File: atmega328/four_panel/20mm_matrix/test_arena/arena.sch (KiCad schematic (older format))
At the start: 35 parts, among them P1 CONN15, P10 CONN_2X2, P11 CONN_2X2, P12 CONN_2X2, P13 CONN_2X2, P14 CONN_2X2, P15 CONN_2X2, P16 CONN_2X2, P17 CONN_2X2, P18 CONN_2X2, P19 CONN_2X2, P2 CONN15, P20 CONN_2X2, P21 CONN_2X2, P22 CONN_20X2, P23 CONN_30X2, P24 CONN_2, P3 CONN15, P4 CONN15, P5 CONN15, P6 CONN15, P7 CONN_2X2, P8 CONN_2X2, P9 CONN_2X2

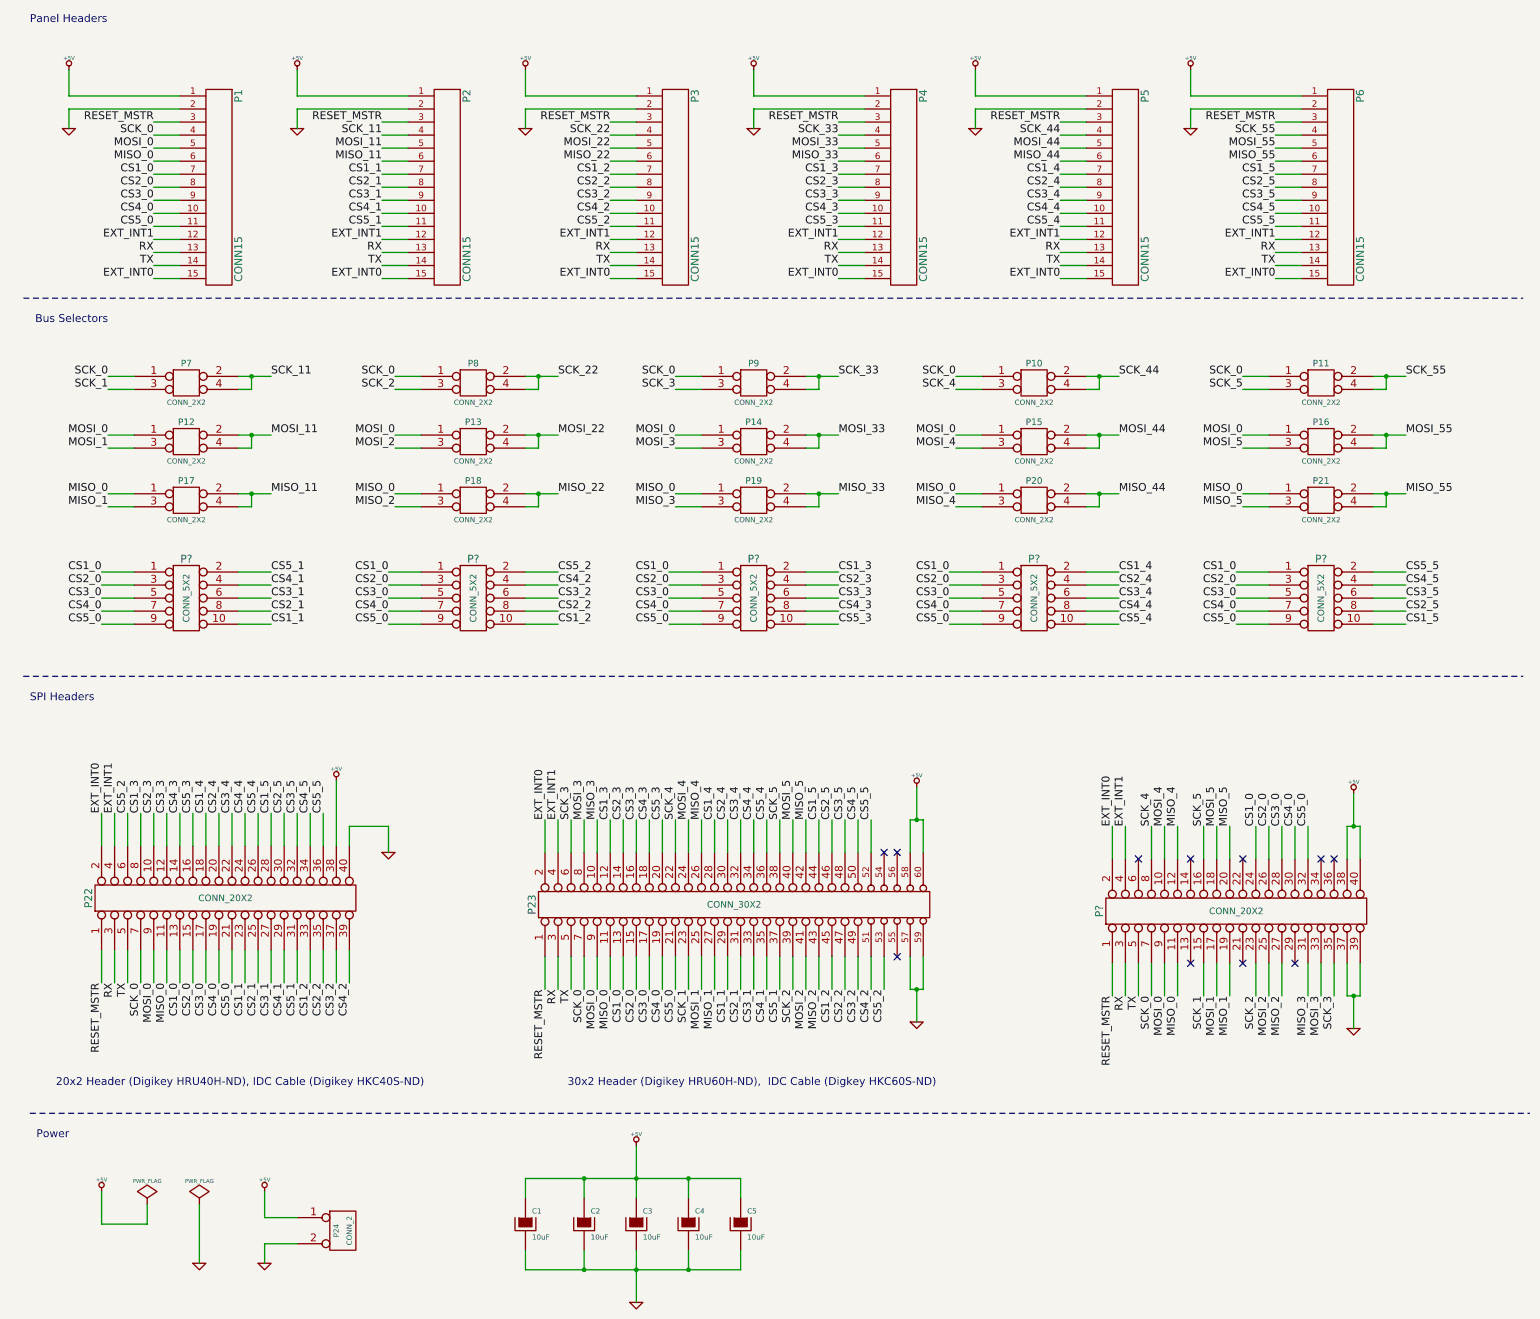
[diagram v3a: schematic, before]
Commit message: Added common CS SPI header to 4x20mm max6960 test arena. Fixed minor issue with 4x20mm atmega328 test arena.
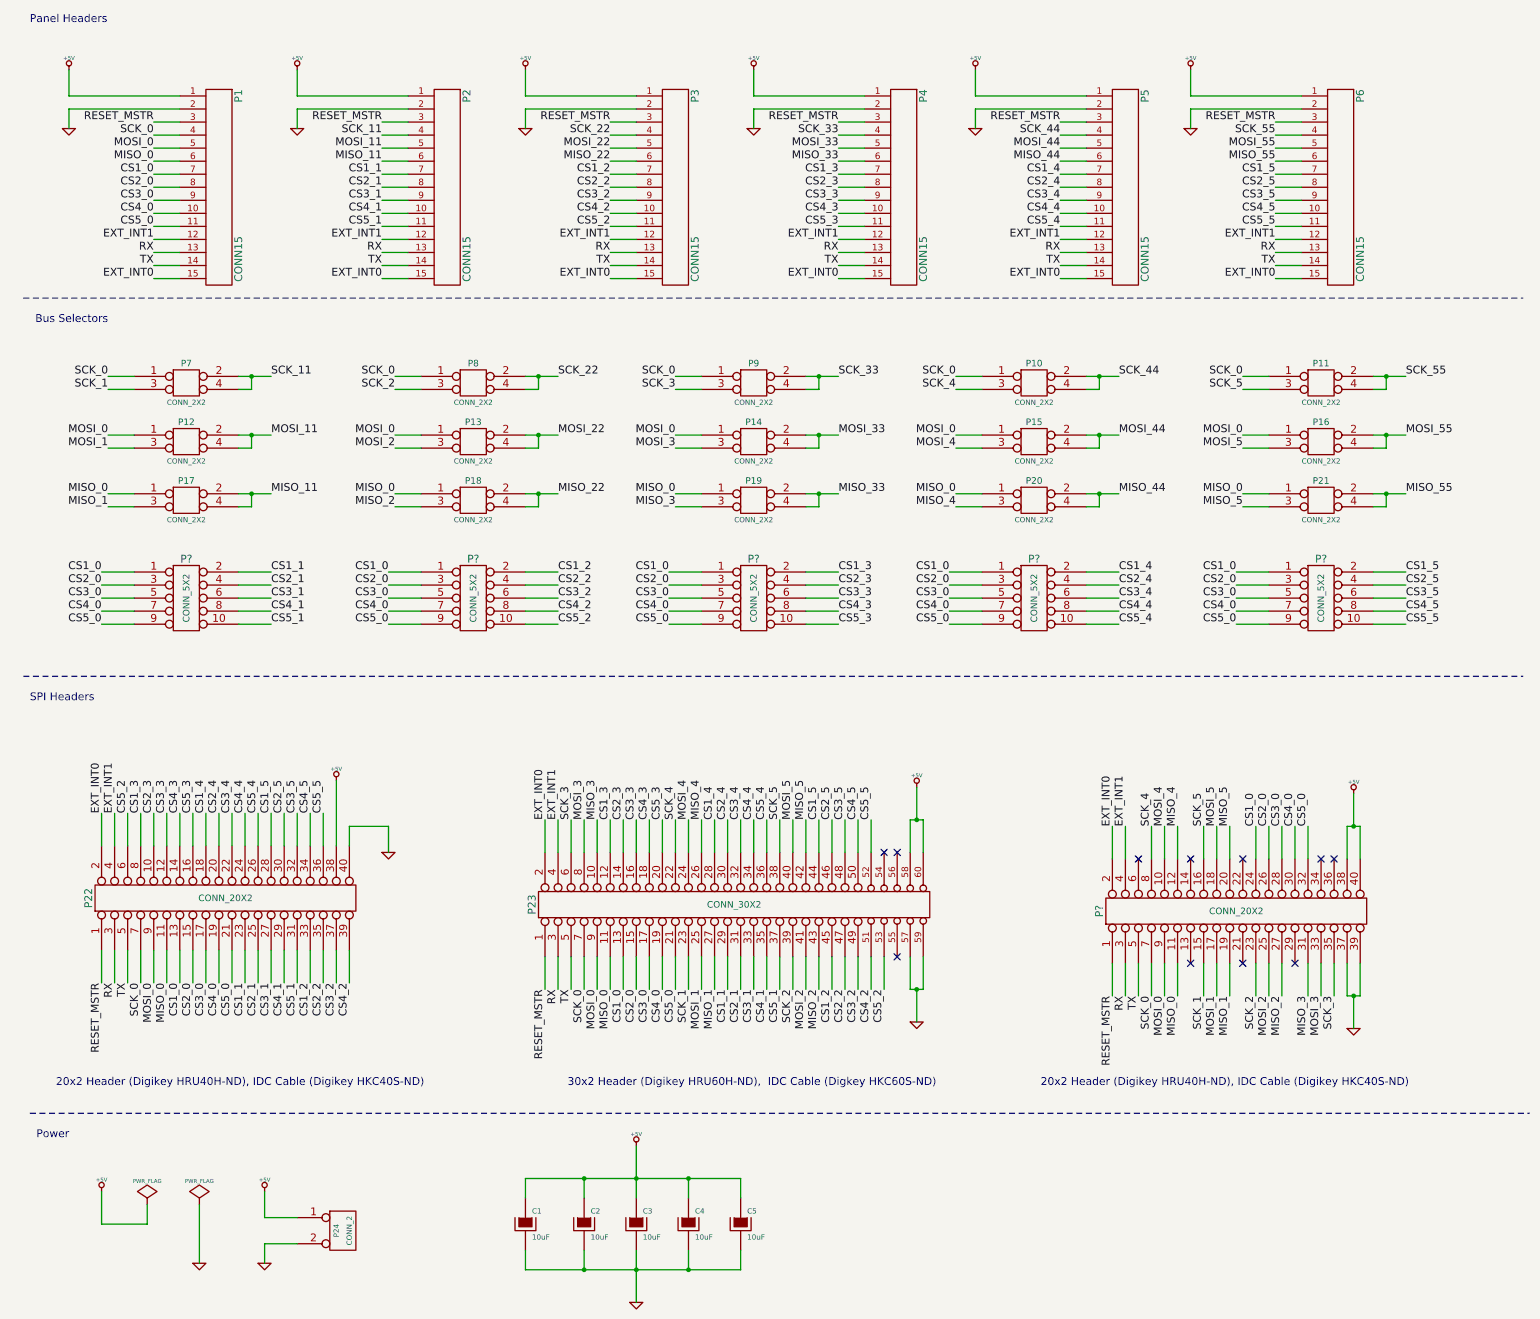
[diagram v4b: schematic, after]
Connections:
- net CS1_1: now also P?.2; no longer P?.10
- net CS1_2: now also P?.2; no longer P?.10
- net CS1_5: now also P?.2; no longer P?.10
- net CS2_1: now also P?.4; no longer P?.8
- net CS2_2: now also P?.4; no longer P?.8
- net CS2_5: now also P?.4; no longer P?.8
- net CS4_1: now also P?.8; no longer P?.4
- net CS4_2: now also P?.8; no longer P?.4
- net CS4_5: now also P?.8; no longer P?.4
- net CS5_1: now also P?.10; no longer P?.2
- net CS5_2: now also P?.10; no longer P?.2
- net CS5_5: now also P?.10; no longer P?.2
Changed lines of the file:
@@
 NoConn ~ 7200 7800
 Wire Wire Line
-	7300 6750 7400 6750
+	7300 6750 7350 6750
+Wire Wire Line
+	7350 6750 7400 6750
 Wire Wire Line
 	7350 6750 7350 6500
 Connection ~ 7350 6750
 Wire Wire Line
-	7300 8050 7400 8050
+	7300 8050 7350 8050
+Wire Wire Line
+	7350 8050 7400 8050
 Wire Wire Line
 	7350 8050 7350 8300
@@
 	1350 3450 1150 3450
 Wire Wire Line
-	2150 3350 2400 3350
+	2150 3350 2250 3350
+Wire Wire Line
+	2250 3350 2400 3350
 Wire Wire Line
 	2250 3350 2250 3450
@@
 	2250 3900 2250 3800
 Wire Wire Line
-	2150 3800 2400 3800
+	2150 3800 2250 3800
+Wire Wire Line
+	2250 3800 2400 3800
 Connection ~ 2250 3800
 Text Label 2400 3800 0    60   ~ 0
@@
 	1350 4350 1150 4350
 Wire Wire Line
-	2150 4250 2400 4250
+	2150 4250 2250 4250
+Wire Wire Line
+	2250 4250 2400 4250
 Wire Wire Line
 	2250 4250 2250 4350
@@
 MISO_2
 Wire Wire Line
-	4350 3350 4600 3350
+	4350 3350 4450 3350
+Wire Wire Line
+	4450 3350 4600 3350
 Wire Wire Line
 	4450 3350 4450 3450
@@
 	4450 3900 4450 3800
 Wire Wire Line
-	4350 3800 4600 3800
+	4350 3800 4450 3800
+Wire Wire Line
+	4450 3800 4600 3800
 Connection ~ 4450 3800
 Text Label 4600 3800 0    60   ~ 0
 MOSI_22
 Wire Wire Line
-	4350 4250 4600 4250
+	4350 4250 4450 4250
+Wire Wire Line
+	4450 4250 4600 4250
 Wire Wire Line
 	4450 4250 4450 4350
@@
 MISO_3
 Wire Wire Line
-	6500 3350 6750 3350
+	6500 3350 6600 3350
+Wire Wire Line
+	6600 3350 6750 3350
 Wire Wire Line
 	6600 3350 6600 3450
@@
 	6600 3900 6600 3800
 Wire Wire Line
-	6500 3800 6750 3800
+	6500 3800 6600 3800
+Wire Wire Line
+	6600 3800 6750 3800
 Connection ~ 6600 3800
 Text Label 6750 3800 0    60   ~ 0
 MOSI_33
 Wire Wire Line
-	6500 4250 6750 4250
+	6500 4250 6600 4250
+Wire Wire Line
+	6600 4250 6750 4250
 Wire Wire Line
 	6600 4250 6600 4350
@@
 MISO_4
 Wire Wire Line
-	8650 3350 8900 3350
+	8650 3350 8750 3350
+Wire Wire Line
+	8750 3350 8900 3350
 Wire Wire Line
 	8750 3350 8750 3450
@@
 	8750 3900 8750 3800
 Wire Wire Line
-	8650 3800 8900 3800
+	8650 3800 8750 3800
+Wire Wire Line
+	8750 3800 8900 3800
 Connection ~ 8750 3800
 Text Label 8900 3800 0    60   ~ 0
 MOSI_44
 Wire Wire Line
-	8650 4250 8900 4250
+	8650 4250 8750 4250
+Wire Wire Line
+	8750 4250 8900 4250
 Wire Wire Line
 	8750 4250 8750 4350
@@
 MISO_5
 Wire Wire Line
-	10850 3350 11100 3350
+	10850 3350 10950 3350
+Wire Wire Line
+	10950 3350 11100 3350
 Wire Wire Line
 	10950 3350 10950 3450
@@
 	10950 3900 10950 3800
 Wire Wire Line
-	10850 3800 11100 3800
+	10850 3800 10950 3800
+Wire Wire Line
+	10950 3800 11100 3800
 Connection ~ 10950 3800
 Text Label 11100 3800 0    60   ~ 0
 MOSI_55
 Wire Wire Line
-	10850 4250 11100 4250
+	10850 4250 10950 4250
+Wire Wire Line
+	10950 4250 11100 4250
 Wire Wire Line
 	10950 4250 10950 4350
@@
 	4350 9650 4350 9500
 Wire Wire Line
-	4350 9500 6000 9500
+	4350 9500 4800 9500
+Wire Wire Line
+	4800 9500 5200 9500
+Wire Wire Line
+	5200 9500 5600 9500
+Wire Wire Line
+	5600 9500 6000 9500
 Wire Wire Line
 	4800 9500 4800 9650
 Wire Wire Line
-	5200 9250 5200 9650
+	5200 9250 5200 9500
+Wire Wire Line
+	5200 9500 5200 9650
 Connection ~ 4800 9500
 Wire Wire Line
@@
 	4350 10050 4350 10200
 Wire Wire Line
-	4350 10200 6000 10200
+	4350 10200 4800 10200
+Wire Wire Line
+	4800 10200 5200 10200
+Wire Wire Line
+	5200 10200 5600 10200
+Wire Wire Line
+	5600 10200 6000 10200
 Wire Wire Line
 	4800 10200 4800 10050
 Wire Wire Line
-	5200 10050 5200 10450
+	5200 10050 5200 10200
+Wire Wire Line
+	5200 10200 5200 10450
 Connection ~ 4800 10200
 Wire Wire Line
@@
 	9350 7850 9350 8100
 Wire Wire Line
+	10850 4850 11100 4850
+Wire Wire Line
+	10850 4950 11100 4950
+Wire Wire Line
+	10850 5050 11100 5050
+Wire Wire Line
+	10850 5150 11100 5150
+Wire Wire Line
 	10850 5250 11100 5250
 Wire Wire Line
-	10850 5150 11100 5150
-Wire Wire Line
-	10850 5050 11100 5050
-Wire Wire Line
-	10850 4950 11100 4950
-Wire Wire Line
-	10850 4850 11100 4850
-Wire Wire Line
 	9550 7850 9550 8100
 Wire Wire Line
@@
 	9750 7850 9750 8100
 Wire Wire Line
+	2150 4850 2400 4850
+Wire Wire Line
+	2150 4950 2400 4950
+Wire Wire Line
+	2150 5050 2400 5050
+Wire Wire Line
+	2150 5150 2400 5150
+Wire Wire Line
 	2150 5250 2400 5250
 Wire Wire Line
-	2150 5150 2400 5150
-Wire Wire Line
-	2150 5050 2400 5050
-Wire Wire Line
-	2150 4950 2400 4950
-Wire Wire Line
-	2150 4850 2400 4850
-Wire Wire Line
 	9950 7850 9950 8100
 Wire Wire Line
@@
 	10150 7850 10150 8100
 Wire Wire Line
+	4350 4850 4600 4850
+Wire Wire Line
+	4350 4950 4600 4950
+Wire Wire Line
+	4350 5050 4600 5050
+Wire Wire Line
+	4350 5150 4600 5150
+Wire Wire Line
 	4350 5250 4600 5250
-Wire Wire Line
-	4350 5150 4600 5150
-Wire Wire Line
-	4350 5050 4600 5050
-Wire Wire Line
-	4350 4950 4600 4950
-Wire Wire Line
-	4350 4850 4600 4850
 Wire Wire Line
 	10650 7850 10650 8100
@@
 Text Label 9350 8100 3    60   ~ 0
 MISO_0
-Text Label 11100 5250 0    60   ~ 0
+Text Label 11100 4850 0    60   ~ 0
 CS1_5
-Text Label 11100 5150 0    60   ~ 0
+Text Label 11100 4950 0    60   ~ 0
 CS2_5
 Text Label 11100 5050 0    60   ~ 0
 CS3_5
-Text Label 11100 4950 0    60   ~ 0
+Text Label 11100 5150 0    60   ~ 0
 CS4_5
-Text Label 11100 4850 0    60   ~ 0
+Text Label 11100 5250 0    60   ~ 0
 CS5_5
 Text Label 9550 8100 3    60   ~ 0
@@
 Text Label 9750 8100 3    60   ~ 0
 MISO_1
-Text Label 2400 5250 0    60   ~ 0
+Text Label 2400 4850 0    60   ~ 0
 CS1_1
-Text Label 2400 5150 0    60   ~ 0
+Text Label 2400 4950 0    60   ~ 0
 CS2_1
 Text Label 2400 5050 0    60   ~ 0
 CS3_1
-Text Label 2400 4950 0    60   ~ 0
+Text Label 2400 5150 0    60   ~ 0
 CS4_1
-Text Label 2400 4850 0    60   ~ 0
+Text Label 2400 5250 0    60   ~ 0
 CS5_1
 Text Label 9950 8100 3    60   ~ 0
@@
 Text Label 10150 8100 3    60   ~ 0
 MISO_2
-Text Label 4600 5250 0    60   ~ 0
+Text Label 4600 4850 0    60   ~ 0
 CS1_2
-Text Label 4600 5150 0    60   ~ 0
+Text Label 4600 4950 0    60   ~ 0
 CS2_2
 Text Label 4600 5050 0    60   ~ 0
 CS3_2
-Text Label 4600 4950 0    60   ~ 0
+Text Label 4600 5150 0    60   ~ 0
 CS4_2
-Text Label 4600 4850 0    60   ~ 0
+Text Label 4600 5250 0    60   ~ 0
 CS5_2
 Wire Wire Line
-	10650 8100 10750 8100
+	10650 8100 10700 8100
+Wire Wire Line
+	10700 8100 10750 8100
 Wire Wire Line
 	10700 8100 10700 8350
@@
 CS5_0
 Wire Wire Line
-	10650 6800 10750 6800
+	10650 6800 10700 6800
+Wire Wire Line
+	10700 6800 10750 6800
 Wire Wire Line
 	10700 6800 10700 6550
@@
 Text Label 9800 5250 2    60   ~ 0
 CS5_0
+Text Notes 8300 8800 0    60   ~ 0
+20x2 Header (Digikey HRU40H-ND), IDC Cable (Digikey HKC40S-ND)
 $EndSCHEMATC
